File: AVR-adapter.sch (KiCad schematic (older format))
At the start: 15 parts, among them CON1 AVR-ISP-6, CON2 BARREL_JACK, IC1 ATMEGA328-P, IC2 ATTINY85-P, IC3 ATTINY2313-P, SW1 SPST, U1 LM7805CT, X1 CRYSTAL

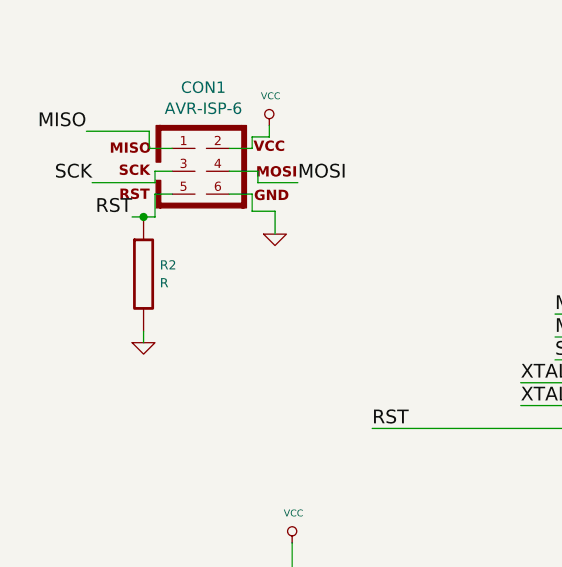
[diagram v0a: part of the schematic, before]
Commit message: Fixed error on pcb-jack
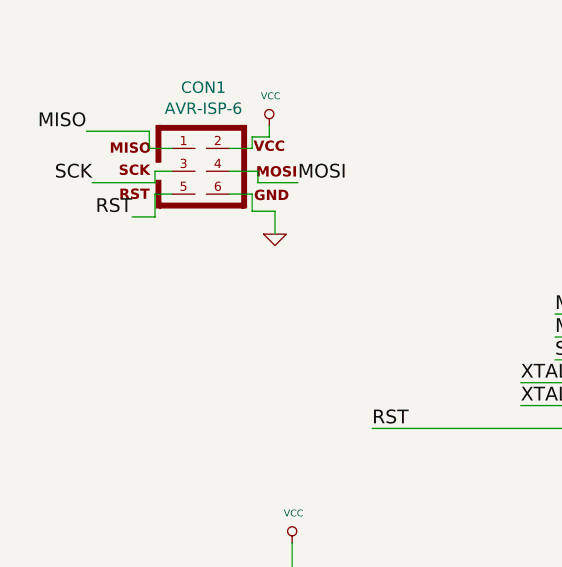
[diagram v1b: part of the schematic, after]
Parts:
- removed R2: R, Discret:R3, symbol R
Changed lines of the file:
@@
 Text Label 6400 4575 0    60   ~ 0
 RST
-Wire Wire Line
-	6450 2575 6450 2500
-Wire Wire Line
-	6450 2500 6425 2500
-Wire Wire Line
-	8425 4875 8425 4750
-Wire Wire Line
-	3725 5325 3625 5325
-Wire Wire Line
-	3625 5325 3625 5500
-Wire Wire Line
-	3725 5425 3625 5425
-Connection ~ 3625 5425
-Wire Wire Line
-	2125 1375 2250 1375
-Wire Wire Line
-	2250 1375 2250 1425
-Wire Wire Line
-	2250 1425 2425 1425
-Wire Wire Line
-	2300 1175 2300 1225
-Wire Wire Line
-	2300 1225 2225 1225
-Wire Wire Line
-	2225 1225 2225 1275
-Wire Wire Line
-	2225 1275 2125 1275
-Wire Wire Line
-	2125 1475 2225 1475
-Wire Wire Line
-	2225 1475 2225 1550
-Wire Wire Line
-	2225 1550 2325 1550
-Wire Wire Line
-	2325 1550 2325 1650
-Wire Wire Line
-	1875 1475 1800 1475
-Wire Wire Line
-	1800 1475 1800 1575
-Wire Wire Line
-	1800 1575 1700 1575
-Wire Wire Line
-	1875 1375 1800 1375
-Wire Wire Line
-	1800 1375 1800 1425
-Wire Wire Line
-	1800 1425 1525 1425
-Wire Wire Line
-	1875 1275 1775 1275
-Wire Wire Line
-	1775 1275 1775 1200
-Wire Wire Line
-	1775 1200 1500 1200
-Wire Wire Line
-	5625 4575 6400 4575
-Wire Wire Line
-	2750 2500 3725 2500
-Wire Wire Line
-	6400 2950 7275 2950
 Text Label 2750 2500 0    60   ~ 0
 RST
-Wire Wire Line
-	3725 2400 3400 2400
-Wire Wire Line
-	3725 2300 3400 2300
 Text Label 3400 2300 0    60   ~ 0
 XTAL1
 Text Label 3400 2400 0    60   ~ 0
 XTAL2
-Wire Wire Line
-	5625 3725 5950 3725
-Wire Wire Line
-	5625 3825 5950 3825
 Text Label 5950 3825 2    60   ~ 0
 XTAL2
 Text Label 5950 3725 2    60   ~ 0
 XTAL1
-Wire Wire Line
-	7275 3250 7050 3250
-Wire Wire Line
-	7275 3450 7050 3450
 Text Label 7050 3450 2    60   ~ 0
 XTAL1
@@
 	-1   0    0    1
 $EndComp
-Wire Wire Line
-	8425 1125 8425 650
-Wire Wire Line
-	7825 1125 7825 650
 Text Label 7825 650  2    60   ~ 0
 XTAL1
 Text Label 8425 650  2    60   ~ 0
 XTAL2
-Connection ~ 8425 950
-Connection ~ 7825 950
 $Comp
 L GND #PWR09
@@
 	1    0    0    -1
 $EndComp
-Wire Wire Line
-	8150 1600 8150 1525
-Wire Wire Line
-	7825 1525 8425 1525
-Connection ~ 8150 1525
-Wire Wire Line
-	3725 2000 3550 2000
-Wire Wire Line
-	3725 2100 3550 2100
-Wire Wire Line
-	3725 2200 3550 2200
 Text Label 3550 2000 0    60   ~ 0
 MOSI
@@
 Text Label 3550 2200 0    60   ~ 0
 SCK
-Wire Wire Line
-	5625 3425 5875 3425
-Wire Wire Line
-	5625 3525 5875 3525
-Wire Wire Line
-	5625 3625 5875 3625
 Text Label 5875 3425 2    60   ~ 0
 MOSI
@@
 Text Label 5875 3625 2    60   ~ 0
 SCK
-Wire Wire Line
-	2400 3125 3725 3125
-Wire Wire Line
-	2400 3000 2400 3125
-Wire Wire Line
-	6425 2000 7125 2000
-Wire Wire Line
-	7125 2000 7125 1800
-Wire Wire Line
-	9175 2625 9175 2475
-Wire Wire Line
-	8425 2625 9175 2625
-Wire Wire Line
-	8425 2625 8425 2650
 $Comp
 L VCC #PWR010
@@
 	1    0    0    -1
 $EndComp
-Wire Wire Line
-	5150 6425 5150 6475
-Wire Wire Line
-	5150 6475 4975 6475
 $Comp
 L VDD #PWR011
@@
 	1    0    0    -1
 $EndComp
-Wire Wire Line
-	4075 6475 4175 6475
 $Comp
 L GND #PWR012
@@
 	1    0    0    -1
 $EndComp
-Wire Wire Line
-	4575 6875 4575 6775
 $Comp
 L VDD #PWR013
@@
 	1    0    0    -1
 $EndComp
-Wire Wire Line
-	2800 6000 2800 6050
-Wire Wire Line
-	2800 6050 2700 6050
-Wire Wire Line
-	2700 6150 2800 6150
-Wire Wire Line
-	2800 6150 2800 6375
-Wire Wire Line
-	2800 6250 2700 6250
-Connection ~ 2800 6250
 $Comp
 L GND #PWR014
@@
 	1    0    0    -1
 $EndComp
-Wire Wire Line
-	3950 7000 4975 7000
 $Comp
 L C C5
@@
 	1    0    0    -1
 $EndComp
-Connection ~ 4675 7000
 $Comp
 L CP1 C6
@@
 	1    0    0    -1
 $EndComp
-Wire Wire Line
-	4975 7400 3950 7400
-Wire Wire Line
-	3950 7400 3950 7500
-Connection ~ 4675 7400
-Wire Wire Line
-	9575 3550 9800 3550
 Text Label 9800 3550 2    60   ~ 0
 MISO
-Wire Wire Line
-	9575 3650 9775 3650
 Text Label 9775 3650 2    60   ~ 0
 SCK
-Wire Wire Line
-	9575 3450 9775 3450
 Text Label 9775 3450 2    60   ~ 0
 MOSI
@@
 	1    0    0    -1
 $EndComp
-Wire Wire Line
-	1275 6350 1275 6425
 $Comp
 L SPST SW1
@@
 	1    0    0    -1
 $EndComp
-Wire Wire Line
-	2975 6300 2975 6475
-Wire Wire Line
-	2975 6475 3075 6475
 $Comp
 L VCC #PWR017
@@
 	1    0    0    -1
 $EndComp
-Wire Wire Line
-	1275 5850 1275 5950
 $Comp
 L GND #PWR018
@@
 $EndComp
 Wire Wire Line
+	6450 2575 6450 2500
+Wire Wire Line
+	6450 2500 6425 2500
+Wire Wire Line
+	8425 4875 8425 4750
+Wire Wire Line
+	3725 5325 3625 5325
+Wire Wire Line
+	3625 5325 3625 5500
+Wire Wire Line
+	3725 5425 3625 5425
+Connection ~ 3625 5425
+Wire Wire Line
+	2125 1375 2250 1375
+Wire Wire Line
+	2250 1375 2250 1425
+Wire Wire Line
+	2250 1425 2425 1425
+Wire Wire Line
+	2300 1175 2300 1225
+Wire Wire Line
+	2300 1225 2225 1225
+Wire Wire Line
+	2225 1225 2225 1275
+Wire Wire Line
+	2225 1275 2125 1275
+Wire Wire Line
+	2125 1475 2225 1475
+Wire Wire Line
+	2225 1475 2225 1550
+Wire Wire Line
+	2225 1550 2325 1550
+Wire Wire Line
+	2325 1550 2325 1650
+Wire Wire Line
+	1875 1475 1800 1475
+Wire Wire Line
+	1800 1475 1800 1575
+Wire Wire Line
+	1875 1375 1800 1375
+Wire Wire Line
+	1800 1375 1800 1425
+Wire Wire Line
+	1800 1425 1525 1425
+Wire Wire Line
+	1875 1275 1775 1275
+Wire Wire Line
+	1775 1275 1775 1200
+Wire Wire Line
+	1775 1200 1500 1200
+Wire Wire Line
+	5625 4575 6400 4575
+Wire Wire Line
+	2750 2500 3725 2500
+Wire Wire Line
+	6400 2950 7275 2950
+Wire Wire Line
+	3725 2400 3400 2400
+Wire Wire Line
+	3725 2300 3400 2300
+Wire Wire Line
+	5625 3725 5950 3725
+Wire Wire Line
+	5625 3825 5950 3825
+Wire Wire Line
+	7275 3250 7050 3250
+Wire Wire Line
+	7275 3450 7050 3450
+Wire Wire Line
+	8425 1125 8425 650
+Wire Wire Line
+	7825 1125 7825 650
+Connection ~ 8425 950
+Connection ~ 7825 950
+Wire Wire Line
+	8150 1600 8150 1525
+Wire Wire Line
+	7825 1525 8425 1525
+Connection ~ 8150 1525
+Wire Wire Line
+	3725 2000 3550 2000
+Wire Wire Line
+	3725 2100 3550 2100
+Wire Wire Line
+	3725 2200 3550 2200
+Wire Wire Line
+	5625 3425 5875 3425
+Wire Wire Line
+	5625 3525 5875 3525
+Wire Wire Line
+	5625 3625 5875 3625
+Wire Wire Line
+	2400 3125 3725 3125
+Wire Wire Line
+	2400 3000 2400 3125
+Wire Wire Line
+	6425 2000 7125 2000
+Wire Wire Line
+	7125 2000 7125 1800
+Wire Wire Line
+	9175 2625 9175 2475
+Wire Wire Line
+	8425 2625 9175 2625
+Wire Wire Line
+	8425 2625 8425 2650
+Wire Wire Line
+	5150 6425 5150 6475
+Wire Wire Line
+	5150 6475 4975 6475
+Wire Wire Line
+	4075 6475 4175 6475
+Wire Wire Line
+	4575 6875 4575 6775
+Wire Wire Line
+	2800 6000 2800 6050
+Wire Wire Line
+	2800 6050 2700 6050
+Wire Wire Line
+	2700 6150 2800 6150
+Wire Wire Line
+	2800 6150 2800 6375
+Wire Wire Line
+	2800 6250 2700 6250
+Connection ~ 2800 6250
+Wire Wire Line
+	3950 7000 4975 7000
+Connection ~ 4675 7000
+Wire Wire Line
+	4975 7400 3950 7400
+Wire Wire Line
+	3950 7400 3950 7500
+Connection ~ 4675 7400
+Wire Wire Line
+	9575 3550 9800 3550
+Wire Wire Line
+	9575 3650 9775 3650
+Wire Wire Line
+	9575 3450 9775 3450
+Wire Wire Line
+	1275 6350 1275 6425
+Wire Wire Line
+	2975 6300 2975 6475
+Wire Wire Line
+	2975 6475 3075 6475
+Wire Wire Line
+	1275 5850 1275 5950
+Wire Wire Line
 	1275 7000 1275 6925
-$Comp
-L R R2
-U 1 1 56BCCED0
-P 1750 1825
-F 0 "R2" H 1821 1864 40  0000 L CNN
-F 1 "R" H 1821 1786 40  0000 L CNN
-F 2 "Discret:R3" V 1680 1825 30  0001 C CNN
-F 3 "" H 1750 1825 30  0000 C CNN
-	1    1750 1825
-	1    0    0    -1
-$EndComp
-Connection ~ 1750 1575
-$Comp
-L GND #PWR019
-U 1 1 56BCCF64
-P 1750 2125
-F 0 "#PWR019" H 1750 2125 30  0001 C CNN
-F 1 "GND" H 1750 2055 30  0001 C CNN
-F 2 "" H 1750 2125 60  0000 C CNN
-F 3 "" H 1750 2125 60  0000 C CNN
-	1    1750 2125
-	1    0    0    -1
-$EndComp
-Wire Wire Line
-	1750 2125 1750 2075
+Wire Wire Line
+	1800 1575 1700 1575
 $EndSCHEMATC

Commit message: New drill-file
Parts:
- CON2: footprint diy_connectors:JACK_2.1_DC -> Connect:BARREL_JACK
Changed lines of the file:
@@
 F 0 "CON2" H 2381 6503 60  0000 C CNN
 F 1 "BARREL_JACK" H 2381 6397 60  0000 C CNN
-F 2 "diy_connectors:JACK_2.1_DC" H 2400 6150 60  0001 C CNN
+F 2 "Connect:BARREL_JACK" H 2400 6150 60  0001 C CNN
 F 3 "" H 2400 6150 60  0000 C CNN
 	1    2400 6150
